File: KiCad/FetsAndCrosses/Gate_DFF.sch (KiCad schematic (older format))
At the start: 0 parts

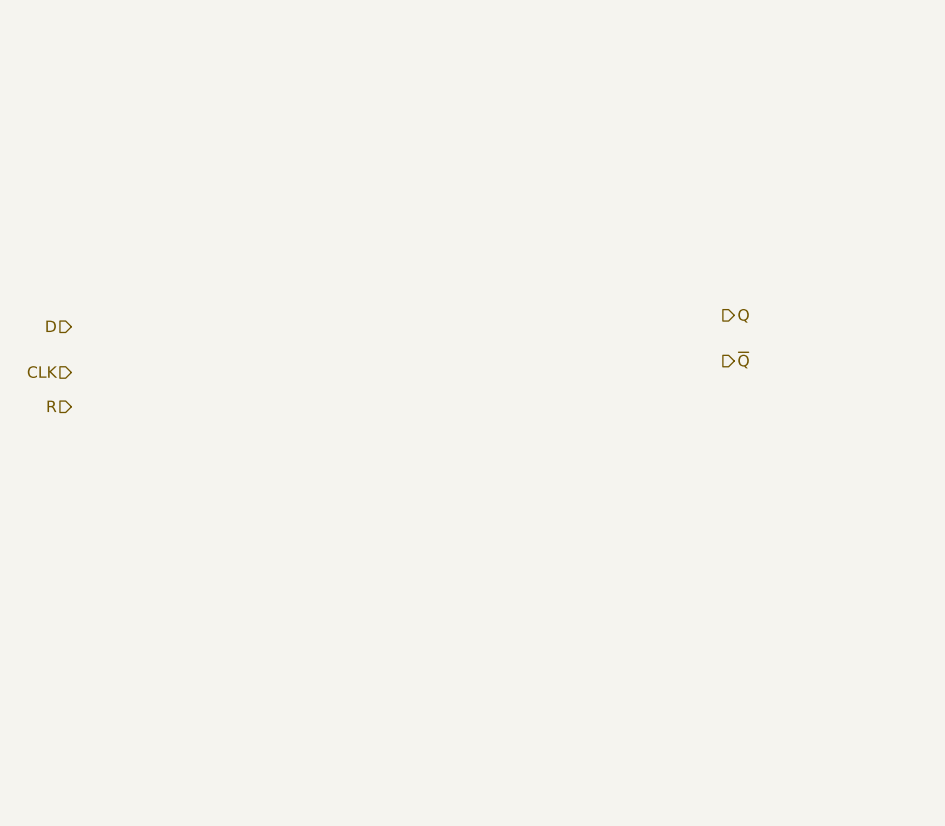
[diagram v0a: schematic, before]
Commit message: Reworked everything to use Buses
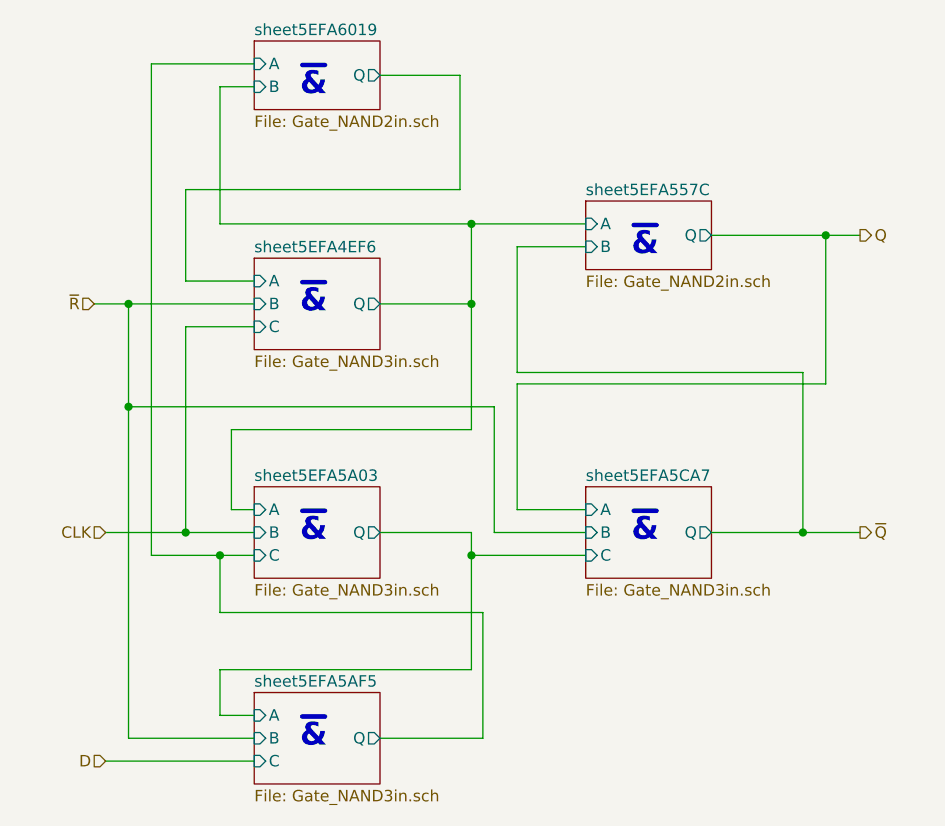
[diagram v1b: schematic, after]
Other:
- note added: "~&"
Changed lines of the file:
@@
 $Descr A4 11693 8268
 encoding utf-8
-Sheet 180 215
+Sheet 69 400
 Title ""
 Date ""
@@
 Comment4 ""
 $EndDescr
-Text HLabel 2700 2850 0    50   Input ~ 0
+Text HLabel 2850 4750 0    50   Input ~ 0
 D
-Text HLabel 2700 3050 0    50   Input ~ 0
+Text HLabel 2850 3750 0    50   Input ~ 0
 CLK
-Text HLabel 2700 3200 0    50   Input ~ 0
-R
-Text HLabel 5550 2800 2    50   Output ~ 0
+Text HLabel 2800 2750 0    50   Input ~ 0
+~R
+Text HLabel 6150 2450 2    50   Output ~ 0
 Q
-Text HLabel 5550 3000 2    50   Output ~ 0
+Text HLabel 6150 3750 2    50   Output ~ 0
 ~Q
+$Sheet
+S 3500 2550 550  400
+U 5EFA4EFC
+F0 "sheet5EFA4EF6" 50
+F1 "Gate_NAND3in.sch" 50
+F2 "A" I L 3500 2650 50
+F3 "B" I L 3500 2750 50
+F4 "C" I L 3500 2850 50
+F5 "Q" O R 4050 2750 50
+$EndSheet
+Text Notes 3700 2800 0    100  ~ 20
+~&
+Text Notes 5150 2550 0    100  ~ 20
+~&
+$Sheet
+S 4950 2300 550  300
+U 5EFA5582
+F0 "sheet5EFA557C" 50
+F1 "Gate_NAND2in.sch" 50
+F2 "Q" O R 5500 2450 50
+F3 "A" I L 4950 2400 50
+F4 "B" I L 4950 2500 50
+$EndSheet
+$Sheet
+S 3500 3550 550  400
+U 5EFA5A09
+F0 "sheet5EFA5A03" 50
+F1 "Gate_NAND3in.sch" 50
+F2 "A" I L 3500 3650 50
+F3 "B" I L 3500 3750 50
+F4 "C" I L 3500 3850 50
+F5 "Q" O R 4050 3750 50
+$EndSheet
+Text Notes 3700 3800 0    100  ~ 20
+~&
+$Sheet
+S 3500 4450 550  400
+U 5EFA5AFB
+F0 "sheet5EFA5AF5" 50
+F1 "Gate_NAND3in.sch" 50
+F2 "A" I L 3500 4550 50
+F3 "B" I L 3500 4650 50
+F4 "C" I L 3500 4750 50
+F5 "Q" O R 4050 4650 50
+$EndSheet
+Text Notes 3700 4700 0    100  ~ 20
+~&
+$Sheet
+S 4950 3550 550  400
+U 5EFA5CAD
+F0 "sheet5EFA5CA7" 50
+F1 "Gate_NAND3in.sch" 50
+F2 "A" I L 4950 3650 50
+F3 "B" I L 4950 3750 50
+F4 "C" I L 4950 3850 50
+F5 "Q" O R 5500 3750 50
+$EndSheet
+Text Notes 5150 3800 0    100  ~ 20
+~&
+Text Notes 3700 1850 0    100  ~ 20
+~&
+$Sheet
+S 3500 1600 550  300
+U 5EFA601F
+F0 "sheet5EFA6019" 50
+F1 "Gate_NAND2in.sch" 50
+F2 "Q" O R 4050 1750 50
+F3 "A" I L 3500 1700 50
+F4 "B" I L 3500 1800 50
+$EndSheet
+Wire Wire Line
+	2850 4750 3500 4750
+Wire Wire Line
+	4050 4650 4500 4650
+Wire Wire Line
+	4500 4650 4500 4100
+Wire Wire Line
+	4500 4100 3350 4100
+Wire Wire Line
+	3350 4100 3350 3850
+Wire Wire Line
+	3350 3850 3500 3850
+Wire Wire Line
+	4050 3750 4450 3750
+Wire Wire Line
+	4450 3750 4450 3850
+Wire Wire Line
+	4450 4350 3350 4350
+Wire Wire Line
+	3350 4350 3350 4550
+Wire Wire Line
+	3350 4550 3500 4550
+Wire Wire Line
+	3350 3850 3050 3850
+Wire Wire Line
+	3050 3850 3050 1700
+Wire Wire Line
+	3050 1700 3500 1700
+Connection ~ 3350 3850
+Wire Wire Line
+	2850 3750 3200 3750
+Wire Wire Line
+	3500 3650 3400 3650
+Wire Wire Line
+	3400 3650 3400 3300
+Wire Wire Line
+	3400 3300 4450 3300
+Wire Wire Line
+	4450 3300 4450 2750
+Wire Wire Line
+	4450 2750 4050 2750
+Wire Wire Line
+	3200 3750 3200 2850
+Wire Wire Line
+	3200 2850 3500 2850
+Connection ~ 3200 3750
+Wire Wire Line
+	3200 3750 3500 3750
+Wire Wire Line
+	2800 2750 2950 2750
+Wire Wire Line
+	2950 2750 2950 3200
+Wire Wire Line
+	2950 4650 3500 4650
+Connection ~ 2950 2750
+Wire Wire Line
+	2950 2750 3500 2750
+Wire Wire Line
+	4950 3850 4450 3850
+Connection ~ 4450 3850
+Wire Wire Line
+	4450 3850 4450 4350
+Wire Wire Line
+	4950 3750 4550 3750
+Wire Wire Line
+	4550 3750 4550 3200
+Wire Wire Line
+	4550 3200 2950 3200
+Connection ~ 2950 3200
+Wire Wire Line
+	2950 3200 2950 4650
+Wire Wire Line
+	4950 3650 4650 3650
+Wire Wire Line
+	4650 3650 4650 3100
+Wire Wire Line
+	4650 3100 6000 3100
+Wire Wire Line
+	6000 3100 6000 2450
+Wire Wire Line
+	6000 2450 5500 2450
+Wire Wire Line
+	5500 3750 5900 3750
+Wire Wire Line
+	5900 3750 5900 3050
+Wire Wire Line
+	5900 3050 4650 3050
+Wire Wire Line
+	4650 3050 4650 2500
+Wire Wire Line
+	4650 2500 4950 2500
+Wire Wire Line
+	6150 2450 6000 2450
+Connection ~ 6000 2450
+Wire Wire Line
+	6150 3750 5900 3750
+Connection ~ 5900 3750
+Wire Wire Line
+	4450 2400 4950 2400
+Wire Wire Line
+	4450 2400 4450 2750
+Connection ~ 4450 2750
+Wire Wire Line
+	4450 2400 3350 2400
+Wire Wire Line
+	3350 2400 3350 1800
+Wire Wire Line
+	3350 1800 3500 1800
+Connection ~ 4450 2400
+Wire Wire Line
+	4050 1750 4400 1750
+Wire Wire Line
+	4400 1750 4400 2250
+Wire Wire Line
+	4400 2250 3200 2250
+Wire Wire Line
+	3200 2250 3200 2650
+Wire Wire Line
+	3200 2650 3500 2650
 $EndSCHEMATC
